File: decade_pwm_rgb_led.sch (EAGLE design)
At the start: 10 parts

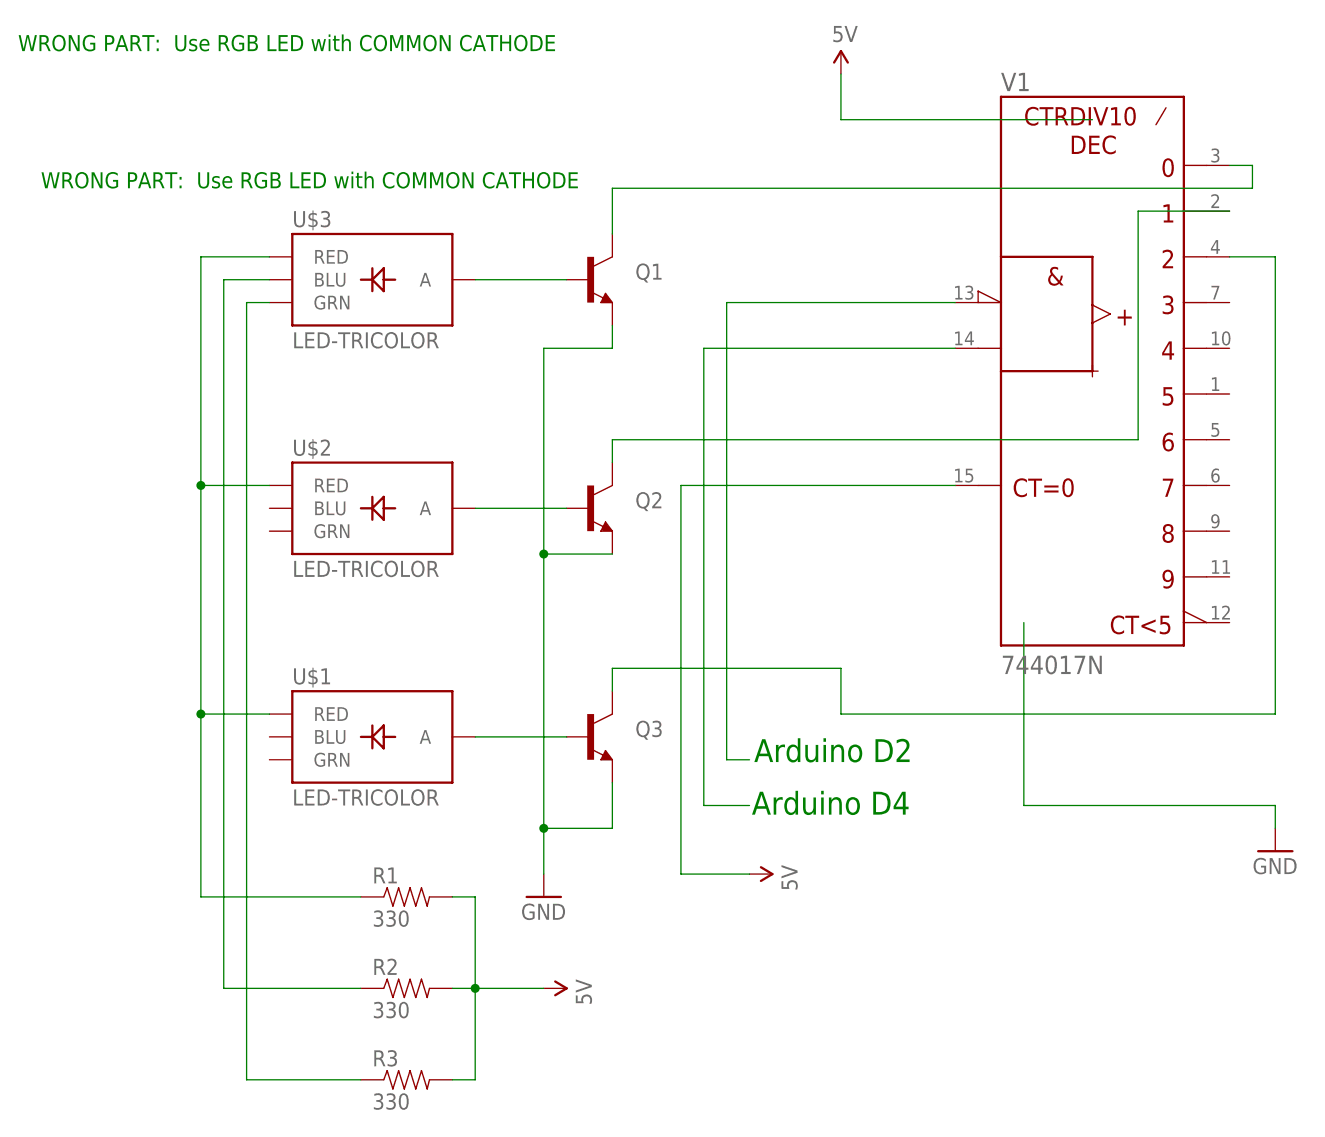
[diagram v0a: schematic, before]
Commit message: update broken schematic, don't know pins tho;
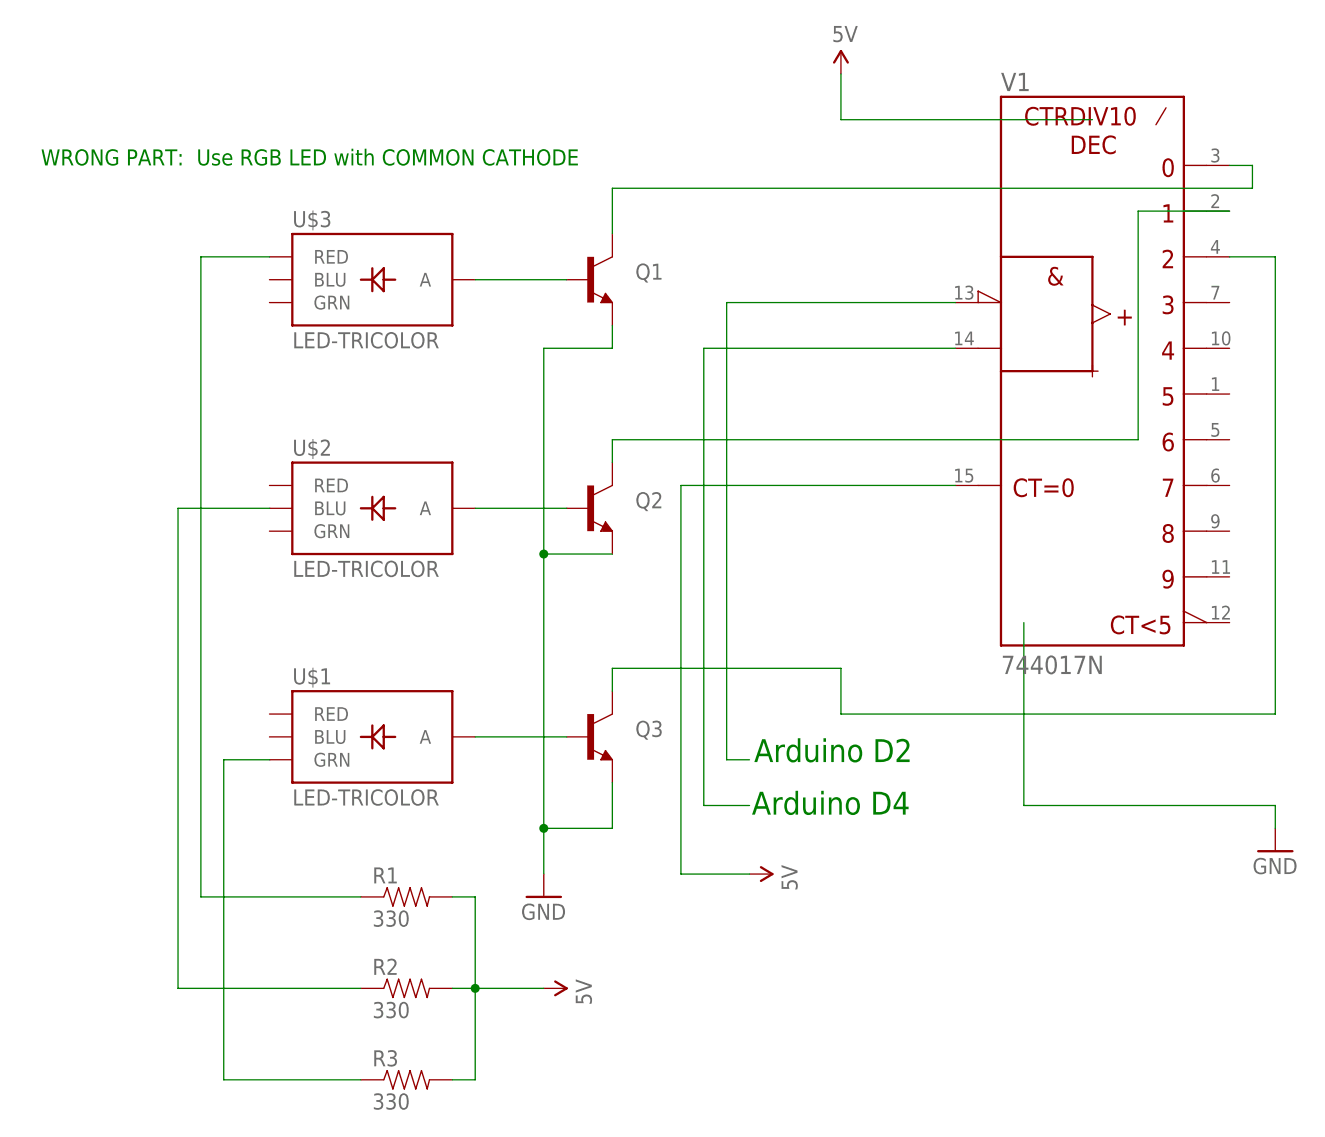
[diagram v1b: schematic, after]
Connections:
- net N$7: no longer U$1.RED, U$2.RED
- net N$8: now also U$2.BLU; no longer U$3.BLU
- net N$9: now also U$1.GRN; no longer U$3.GRN
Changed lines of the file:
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@@
 <?xml version="1.0" encoding="utf-8"?>
 <!DOCTYPE eagle SYSTEM "eagle.dtd">
-<eagle version="6.2">
+<eagle version="6.4">
 <drawing>
 <settings>
@@
 <sheet>
 <plain>
-<text x="5.08" y="124.46" size="1.778" layer="91">WRONG PART:  Use RGB LED with COMMON CATHODE</text>
-<text x="7.62" y="109.22" size="1.778" layer="91">WRONG PART:  Use RGB LED with COMMON CATHODE</text>
+<text x="7.62" y="111.76" size="1.778" layer="91">WRONG PART:  Use RGB LED with COMMON CATHODE</text>
 <text x="86.868" y="45.466" size="2.54" layer="91">Arduino D2</text>
 <text x="86.614" y="39.624" size="2.54" layer="91">Arduino D4</text>
@@
 <pinref part="U$3" gate="G$1" pin="RED"/>
 <wire x1="33.02" y1="101.6" x2="25.4" y2="101.6" width="0.1524" layer="91"/>
-<wire x1="25.4" y1="101.6" x2="25.4" y2="76.2" width="0.1524" layer="91"/>
 <pinref part="R1" gate="G$1" pin="1"/>
-<wire x1="25.4" y1="76.2" x2="25.4" y2="50.8" width="0.1524" layer="91"/>
-<wire x1="25.4" y1="50.8" x2="25.4" y2="30.48" width="0.1524" layer="91"/>
+<wire x1="25.4" y1="101.6" x2="25.4" y2="30.48" width="0.1524" layer="91"/>
 <wire x1="25.4" y1="30.48" x2="43.18" y2="30.48" width="0.1524" layer="91"/>
-<pinref part="U$2" gate="G$1" pin="RED"/>
-<wire x1="33.02" y1="76.2" x2="25.4" y2="76.2" width="0.1524" layer="91"/>
-<junction x="25.4" y="76.2"/>
-<pinref part="U$1" gate="G$1" pin="RED"/>
-<wire x1="33.02" y1="50.8" x2="25.4" y2="50.8" width="0.1524" layer="91"/>
-<junction x="25.4" y="50.8"/>
 </segment>
 </net>
 <net name="N$8" class="0">
 <segment>
-<pinref part="U$3" gate="G$1" pin="BLU"/>
-<wire x1="33.02" y1="99.06" x2="27.94" y2="99.06" width="0.1524" layer="91"/>
-<wire x1="27.94" y1="99.06" x2="27.94" y2="20.32" width="0.1524" layer="91"/>
 <pinref part="R2" gate="G$1" pin="1"/>
-<wire x1="27.94" y1="20.32" x2="43.18" y2="20.32" width="0.1524" layer="91"/>
+<wire x1="22.86" y1="20.32" x2="43.18" y2="20.32" width="0.1524" layer="91"/>
+<pinref part="U$2" gate="G$1" pin="BLU"/>
+<wire x1="33.02" y1="73.66" x2="22.86" y2="73.66" width="0.1524" layer="91"/>
+<wire x1="22.86" y1="73.66" x2="22.86" y2="20.32" width="0.1524" layer="91"/>
 </segment>
 </net>
 <net name="N$9" class="0">
 <segment>
-<pinref part="U$3" gate="G$1" pin="GRN"/>
-<wire x1="33.02" y1="96.52" x2="30.48" y2="96.52" width="0.1524" layer="91"/>
-<wire x1="30.48" y1="96.52" x2="30.48" y2="10.16" width="0.1524" layer="91"/>
 <pinref part="R3" gate="G$1" pin="1"/>
-<wire x1="30.48" y1="10.16" x2="43.18" y2="10.16" width="0.1524" layer="91"/>
-</segment>
-</net>
+<wire x1="27.94" y1="10.16" x2="43.18" y2="10.16" width="0.1524" layer="91"/>
+<pinref part="U$1" gate="G$1" pin="GRN"/>
+<wire x1="33.02" y1="45.72" x2="27.94" y2="45.72" width="0.1524" layer="91"/>
+<wire x1="27.94" y1="45.72" x2="27.94" y2="10.16" width="0.1524" layer="91"/>
+</segment>
+</net>

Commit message: updated schematic;
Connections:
- net N$10 renamed ARDUINO_D1
- net N$11 renamed ARDUINO_D2
- new net ARDUINO_PWM1: R1.2
- new net ARDUINO_PWM2: R2.2
- new net ARDUINO_PWM3: R3.2
- net 5V: no longer R1.2, R2.2, R3.2
- net N$7: now also U$1.RED, U$2.RED
- net N$8: now also U$1.BLU, U$3.BLU
- net N$9: now also U$2.GRN, U$3.GRN
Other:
- note removed: "Arduino D2"
- note removed: "Arduino D4"
- moved on the sheet: R1, R2, R3
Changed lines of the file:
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@@
 <part name="GND2" library="SparkFun" deviceset="GND" device=""/>
 <part name="U$4" library="SparkFun" deviceset="5V" device=""/>
-<part name="U$5" library="SparkFun" deviceset="5V" device=""/>
 <part name="R1" library="SparkFun" deviceset="RESISTOR" device="PTH-1/4W" value="330"/>
 <part name="R2" library="SparkFun" deviceset="RESISTOR" device="PTH-1/4W" value="330"/>
@@
 <plain>
 <text x="7.62" y="111.76" size="1.778" layer="91">WRONG PART:  Use RGB LED with COMMON CATHODE</text>
-<text x="86.868" y="45.466" size="2.54" layer="91">Arduino D2</text>
-<text x="86.614" y="39.624" size="2.54" layer="91">Arduino D4</text>
 </plain>
 <instances>
@@
 <instance part="Q3" gate="G$1" x="68.58" y="48.26"/>
 <instance part="FRAME1" gate="G$1" x="0" y="0"/>
-<instance part="GND1" gate="1" x="63.5" y="30.48"/>
+<instance part="GND1" gate="1" x="63.5" y="35.56"/>
 <instance part="GND2" gate="1" x="144.78" y="35.56"/>
 <instance part="U$4" gate="G$1" x="96.52" y="121.92"/>
-<instance part="U$5" gate="G$1" x="63.5" y="20.32" rot="R270"/>
-<instance part="R1" gate="G$1" x="48.26" y="30.48"/>
-<instance part="R2" gate="G$1" x="48.26" y="20.32"/>
-<instance part="R3" gate="G$1" x="48.26" y="10.16"/>
+<instance part="R1" gate="G$1" x="40.64" y="30.48"/>
+<instance part="R2" gate="G$1" x="40.64" y="20.32"/>
+<instance part="R3" gate="G$1" x="40.64" y="10.16"/>
 <instance part="U$6" gate="G$1" x="86.36" y="33.02" rot="R270"/>
 </instances>
@@
 <segment>
 <pinref part="Q3" gate="G$1" pin="E"/>
-<wire x1="71.12" y1="43.18" x2="71.12" y2="38.1" width="0.1524" layer="91"/>
+<wire x1="71.12" y1="43.18" x2="71.12" y2="40.64" width="0.1524" layer="91"/>
 <pinref part="GND1" gate="1" pin="GND"/>
-<wire x1="71.12" y1="38.1" x2="63.5" y2="38.1" width="0.1524" layer="91"/>
-<wire x1="63.5" y1="38.1" x2="63.5" y2="33.02" width="0.1524" layer="91"/>
+<wire x1="71.12" y1="40.64" x2="63.5" y2="40.64" width="0.1524" layer="91"/>
+<wire x1="63.5" y1="40.64" x2="63.5" y2="38.1" width="0.1524" layer="91"/>
 <pinref part="Q2" gate="G$1" pin="E"/>
 <wire x1="71.12" y1="68.58" x2="63.5" y2="68.58" width="0.1524" layer="91"/>
-<wire x1="63.5" y1="68.58" x2="63.5" y2="38.1" width="0.1524" layer="91"/>
-<junction x="63.5" y="38.1"/>
+<wire x1="63.5" y1="68.58" x2="63.5" y2="40.64" width="0.1524" layer="91"/>
+<junction x="63.5" y="40.64"/>
 <pinref part="Q1" gate="G$1" pin="E"/>
 <wire x1="71.12" y1="93.98" x2="71.12" y2="91.44" width="0.1524" layer="91"/>
@@
 <wire x1="33.02" y1="101.6" x2="25.4" y2="101.6" width="0.1524" layer="91"/>
 <pinref part="R1" gate="G$1" pin="1"/>
-<wire x1="25.4" y1="101.6" x2="25.4" y2="30.48" width="0.1524" layer="91"/>
-<wire x1="25.4" y1="30.48" x2="43.18" y2="30.48" width="0.1524" layer="91"/>
+<wire x1="25.4" y1="101.6" x2="25.4" y2="76.2" width="0.1524" layer="91"/>
+<wire x1="25.4" y1="76.2" x2="25.4" y2="50.8" width="0.1524" layer="91"/>
+<wire x1="25.4" y1="50.8" x2="25.4" y2="30.48" width="0.1524" layer="91"/>
+<wire x1="25.4" y1="30.48" x2="35.56" y2="30.48" width="0.1524" layer="91"/>
+<pinref part="U$2" gate="G$1" pin="RED"/>
+<wire x1="33.02" y1="76.2" x2="25.4" y2="76.2" width="0.1524" layer="91"/>
+<junction x="25.4" y="76.2"/>
+<pinref part="U$1" gate="G$1" pin="RED"/>
+<wire x1="33.02" y1="50.8" x2="25.4" y2="50.8" width="0.1524" layer="91"/>
+<junction x="25.4" y="50.8"/>
 </segment>
 </net>
@@
 <segment>
 <pinref part="R2" gate="G$1" pin="1"/>
-<wire x1="22.86" y1="20.32" x2="43.18" y2="20.32" width="0.1524" layer="91"/>
+<wire x1="22.86" y1="20.32" x2="35.56" y2="20.32" width="0.1524" layer="91"/>
 <pinref part="U$2" gate="G$1" pin="BLU"/>
 <wire x1="33.02" y1="73.66" x2="22.86" y2="73.66" width="0.1524" layer="91"/>
-<wire x1="22.86" y1="73.66" x2="22.86" y2="20.32" width="0.1524" layer="91"/>
+<wire x1="22.86" y1="73.66" x2="22.86" y2="48.26" width="0.1524" layer="91"/>
+<pinref part="U$3" gate="G$1" pin="BLU"/>
+<wire x1="22.86" y1="48.26" x2="22.86" y2="20.32" width="0.1524" layer="91"/>
+<wire x1="33.02" y1="99.06" x2="22.86" y2="99.06" width="0.1524" layer="91"/>
+<wire x1="22.86" y1="99.06" x2="22.86" y2="73.66" width="0.1524" layer="91"/>
+<junction x="22.86" y="73.66"/>
+<pinref part="U$1" gate="G$1" pin="BLU"/>
+<wire x1="33.02" y1="48.26" x2="22.86" y2="48.26" width="0.1524" layer="91"/>
+<junction x="22.86" y="48.26"/>
 </segment>
 </net>
@@
 <segment>
 <pinref part="R3" gate="G$1" pin="1"/>
-<wire x1="27.94" y1="10.16" x2="43.18" y2="10.16" width="0.1524" layer="91"/>
+<wire x1="27.94" y1="10.16" x2="35.56" y2="10.16" width="0.1524" layer="91"/>
 <pinref part="U$1" gate="G$1" pin="GRN"/>
 <wire x1="33.02" y1="45.72" x2="27.94" y2="45.72" width="0.1524" layer="91"/>
 <wire x1="27.94" y1="45.72" x2="27.94" y2="10.16" width="0.1524" layer="91"/>
+<pinref part="U$2" gate="G$1" pin="GRN"/>
+<wire x1="33.02" y1="71.12" x2="27.94" y2="71.12" width="0.1524" layer="91"/>
+<wire x1="27.94" y1="71.12" x2="27.94" y2="45.72" width="0.1524" layer="91"/>
+<junction x="27.94" y="45.72"/>
+<pinref part="U$3" gate="G$1" pin="GRN"/>
+<wire x1="33.02" y1="96.52" x2="27.94" y2="96.52" width="0.1524" layer="91"/>
+<wire x1="27.94" y1="96.52" x2="27.94" y2="71.12" width="0.1524" layer="91"/>
+<junction x="27.94" y="71.12"/>
 </segment>
 </net>
 <net name="5V" class="0">
-<segment>
-<pinref part="R1" gate="G$1" pin="2"/>
-<wire x1="53.34" y1="30.48" x2="55.88" y2="30.48" width="0.1524" layer="91"/>
-<wire x1="55.88" y1="30.48" x2="55.88" y2="20.32" width="0.1524" layer="91"/>
-<pinref part="U$5" gate="G$1" pin="5V"/>
-<wire x1="55.88" y1="20.32" x2="63.5" y2="20.32" width="0.1524" layer="91"/>
-<pinref part="R2" gate="G$1" pin="2"/>
-<wire x1="53.34" y1="20.32" x2="55.88" y2="20.32" width="0.1524" layer="91"/>
-<junction x="55.88" y="20.32"/>
-<pinref part="R3" gate="G$1" pin="2"/>
-<wire x1="53.34" y1="10.16" x2="55.88" y2="10.16" width="0.1524" layer="91"/>
-<wire x1="55.88" y1="10.16" x2="55.88" y2="20.32" width="0.1524" layer="91"/>
-</segment>
 <segment>
 <pinref part="U$4" gate="G$1" pin="5V"/>
@@
 </segment>
 </net>
-<net name="N$10" class="0">
+<net name="ARDUINO_D1" class="0">
 <segment>
 <pinref part="V1" gate="1" pin="!CLKEN"/>
@@
 <wire x1="83.82" y1="96.52" x2="83.82" y2="45.72" width="0.1524" layer="91"/>
 <wire x1="83.82" y1="45.72" x2="86.36" y2="45.72" width="0.1524" layer="91"/>
-</segment>
-</net>
-<net name="N$11" class="0">
+<label x="86.36" y="45.72" size="2.54" layer="95"/>
+</segment>
+</net>
+<net name="ARDUINO_D2" class="0">
 <segment>
 <pinref part="V1" gate="1" pin="CLK"/>
@@
 <wire x1="81.28" y1="91.44" x2="81.28" y2="40.64" width="0.1524" layer="91"/>
 <wire x1="81.28" y1="40.64" x2="86.36" y2="40.64" width="0.1524" layer="91"/>
-</segment>
-</net>
+<label x="86.36" y="40.64" size="2.54" layer="95"/>
+</segment>
+</net>
+<net name="ARDUINO_PWM1" class="0">
+<segment>
+<pinref part="R1" gate="G$1" pin="2"/>
+<wire x1="45.72" y1="30.48" x2="55.88" y2="30.48" width="0.1524" layer="91"/>
+<label x="50.8" y="30.48" size="2.54" layer="95"/>
+</segment>
+</net>
+<net name="ARDUINO_PWM2" class="0">
+<segment>
+<pinref part="R2" gate="G$1" pin="2"/>
+<wire x1="45.72" y1="20.32" x2="55.88" y2="20.32" width="0.1524" layer="91"/>
+<label x="50.8" y="20.32" size="2.54" layer="95"/>
+</segment>
+</net>
+<net name="ARDUINO_PWM3" class="0">
+<segment>
+<pinref part="R3" gate="G$1" pin="2"/>
+<wire x1="45.72" y1="10.16" x2="55.88" y2="10.16" width="0.1524" layer="91"/>
+<label x="50.8" y="10.16" size="2.54" layer="95"/>
+</segment>
+</net>
